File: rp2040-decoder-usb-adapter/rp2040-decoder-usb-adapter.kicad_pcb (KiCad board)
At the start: 2 copper layers, 42 x 16.8 mm, 14 parts, among them J1 505070-2422, J2 SWD, J3 SPEAKER, J4 MISC1, J8 RAIL_PADS, P1 USB_C_Receptacle_USB2.0_16P

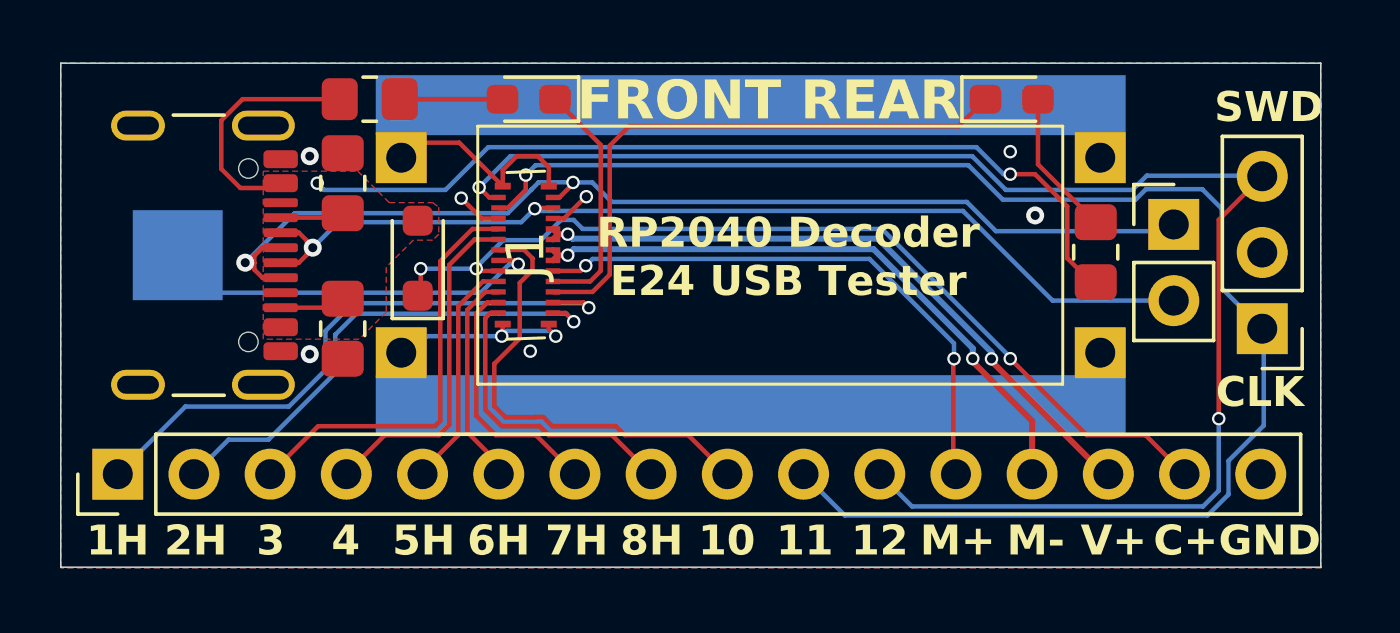
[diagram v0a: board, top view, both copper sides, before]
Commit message: feat: move usb port to avoid shorting rails
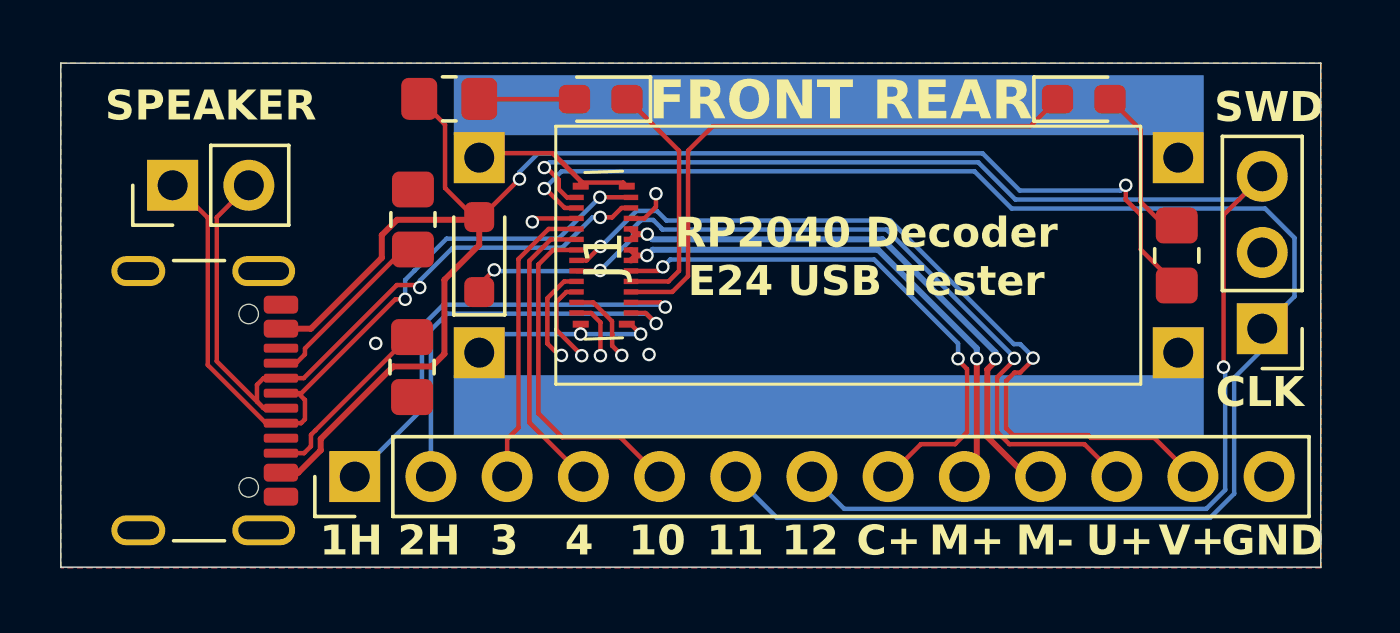
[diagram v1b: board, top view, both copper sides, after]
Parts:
- removed TP1: VCC, TestPoint:TestPoint_Pad_3.0x3.0mm
- J4: footprint Connector_PinHeader_2.54mm:PinHeader_1x16_P2.54mm_Vertical -> Connector_PinHeader_2.54mm:PinHeader_1x13_P2.54mm_Vertical
- moved J3 33.4 mm to (143.5, 79.6), turned to 90 degrees
- moved J4 7.90 mm to (149.6, 89.3)
- moved P1 4.85 mm to (143.5, 86.8)
- moved R4 2.70 mm to (177.0, 82.0)
- moved R3 2.65 mm to (152.8, 76.7)
- moved R2 2.64 mm to (151.5, 85.7)
- moved R1 2.63 mm to (151.5, 80.8)
- moved J1 2.60 mm to (157.9, 82.0)
- moved J8 2.60 mm to (165.4, 82.0)
- moved D2 2.40 mm to (157.8, 76.8)
- moved D3 2.40 mm to (173.9, 76.8)
- moved D1 2.05 mm to (153.8, 81.9)
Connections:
- J4 pad 10: /AUX11 -> /MOTOR_B
- J4 pad 11: /AUX12 -> VDC
- J4 pad 12: /CAP+ -> VCC
- J4 pad 13: /MOTOR_A -> GND
- J4 pad 5: /AUX5 (VDC) -> /AUX10
- J4 pad 6: /AUX6 (VDC) -> /AUX11
- J4 pad 7: /AUX7 (VDC) -> /AUX12
- J4 pad 8: /AUX8 (VDC) -> /CAP+
- J4 pad 9: /AUX10 -> /MOTOR_A
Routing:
- net +5V: track 37.7 -> 53.0 mm
- net VCC: track 13.0 -> 27.7 mm, vias 1 -> 2
- net /D+: track 36.5 -> 26.3 mm
- net /D-: track 33.8 -> 25.7 mm
- net /AUX8 (VDC): track 9.99 -> 2.04 mm, vias 0 -> 1
- net /AUX7 (VDC): track 8.40 -> 2.72 mm, vias 0 -> 1
- net /AUX1 (VDC): track 20.2 -> 15.6 mm
- net /AUX5 (VDC): track 7.78 -> 3.35 mm, vias 0 -> 1
- net /AUX3: track 14.1 -> 9.76 mm
- net /AUX6 (VDC): track 7.20 -> 2.95 mm, vias 0 -> 1
- net /AUX10: track 15.4 -> 11.3 mm
- net Net-(P1-CC2): track 2.16 -> 6.20 mm
- net Net-(P1-CC1): track 2.19 -> 6.08 mm
- net /MOTOR_A: track 20.8 -> 17.7 mm
- net /MOTOR_B: track 22.3 -> 19.4 mm
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- removed copper zone on F.Cu, net +5V
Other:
- board text added: "SPEAKER"
- board text added: "U+"
- board text removed: "5H"
- board text removed: "6H"
- board text removed: "7H"
- board text removed: "8H"
